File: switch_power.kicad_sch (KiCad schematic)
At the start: 31 parts, among them U1 LAN96455F-I/8MW

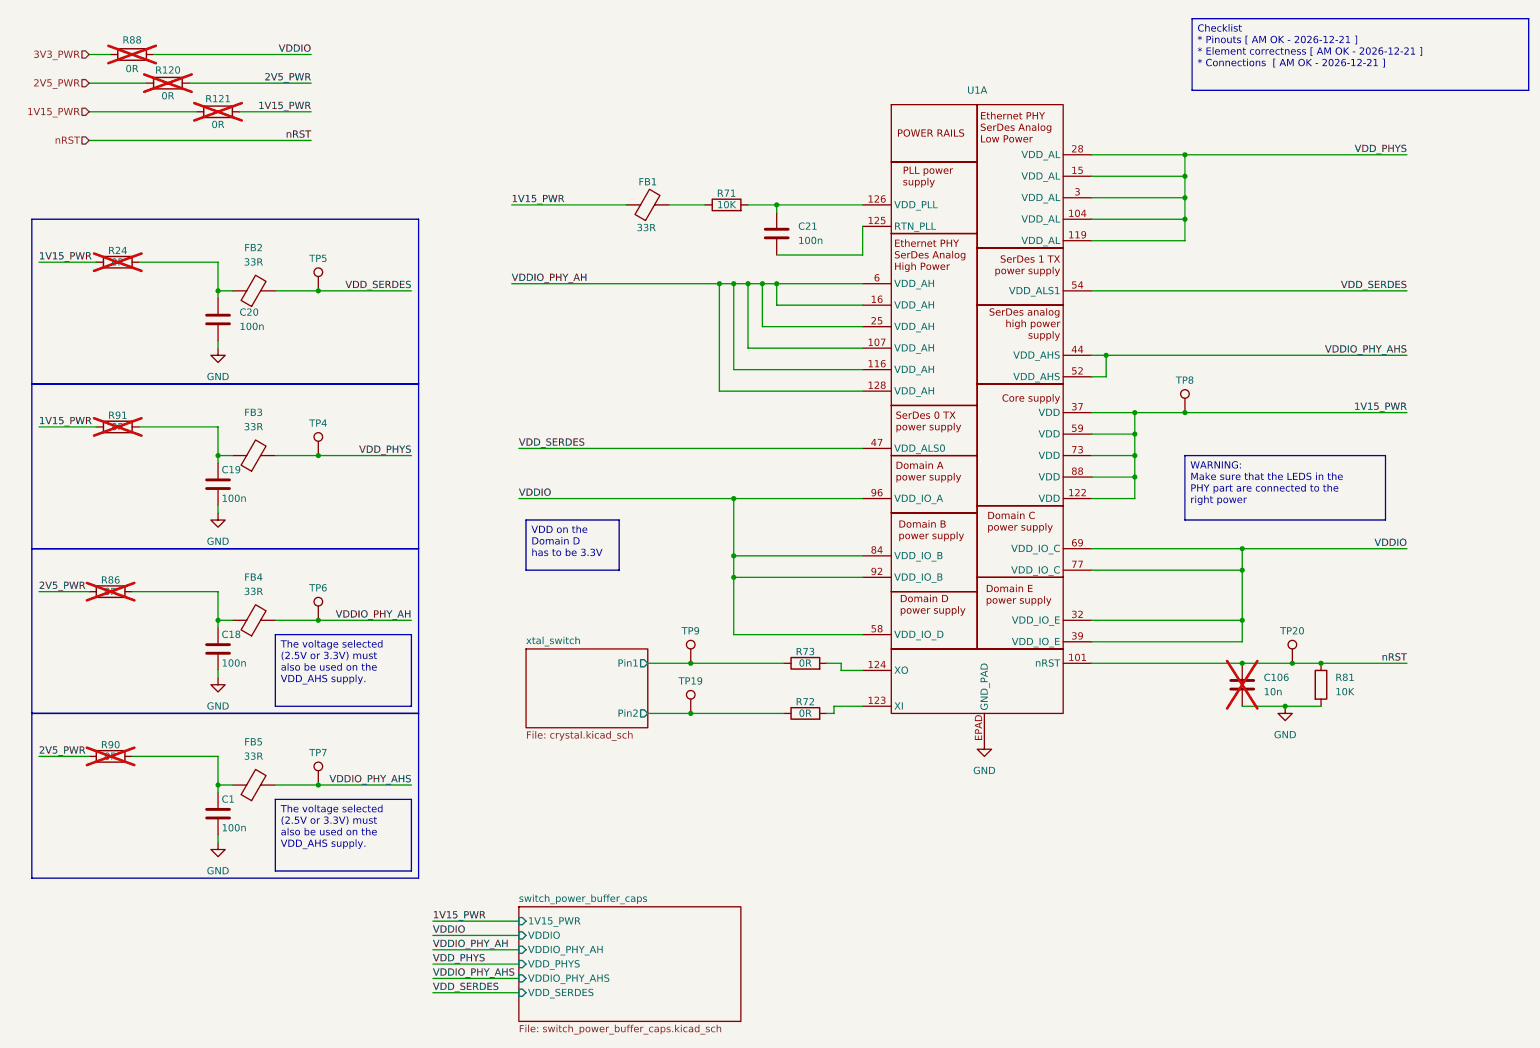
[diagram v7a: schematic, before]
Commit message: updates symbols and fixes ERC errors. Refs: #9
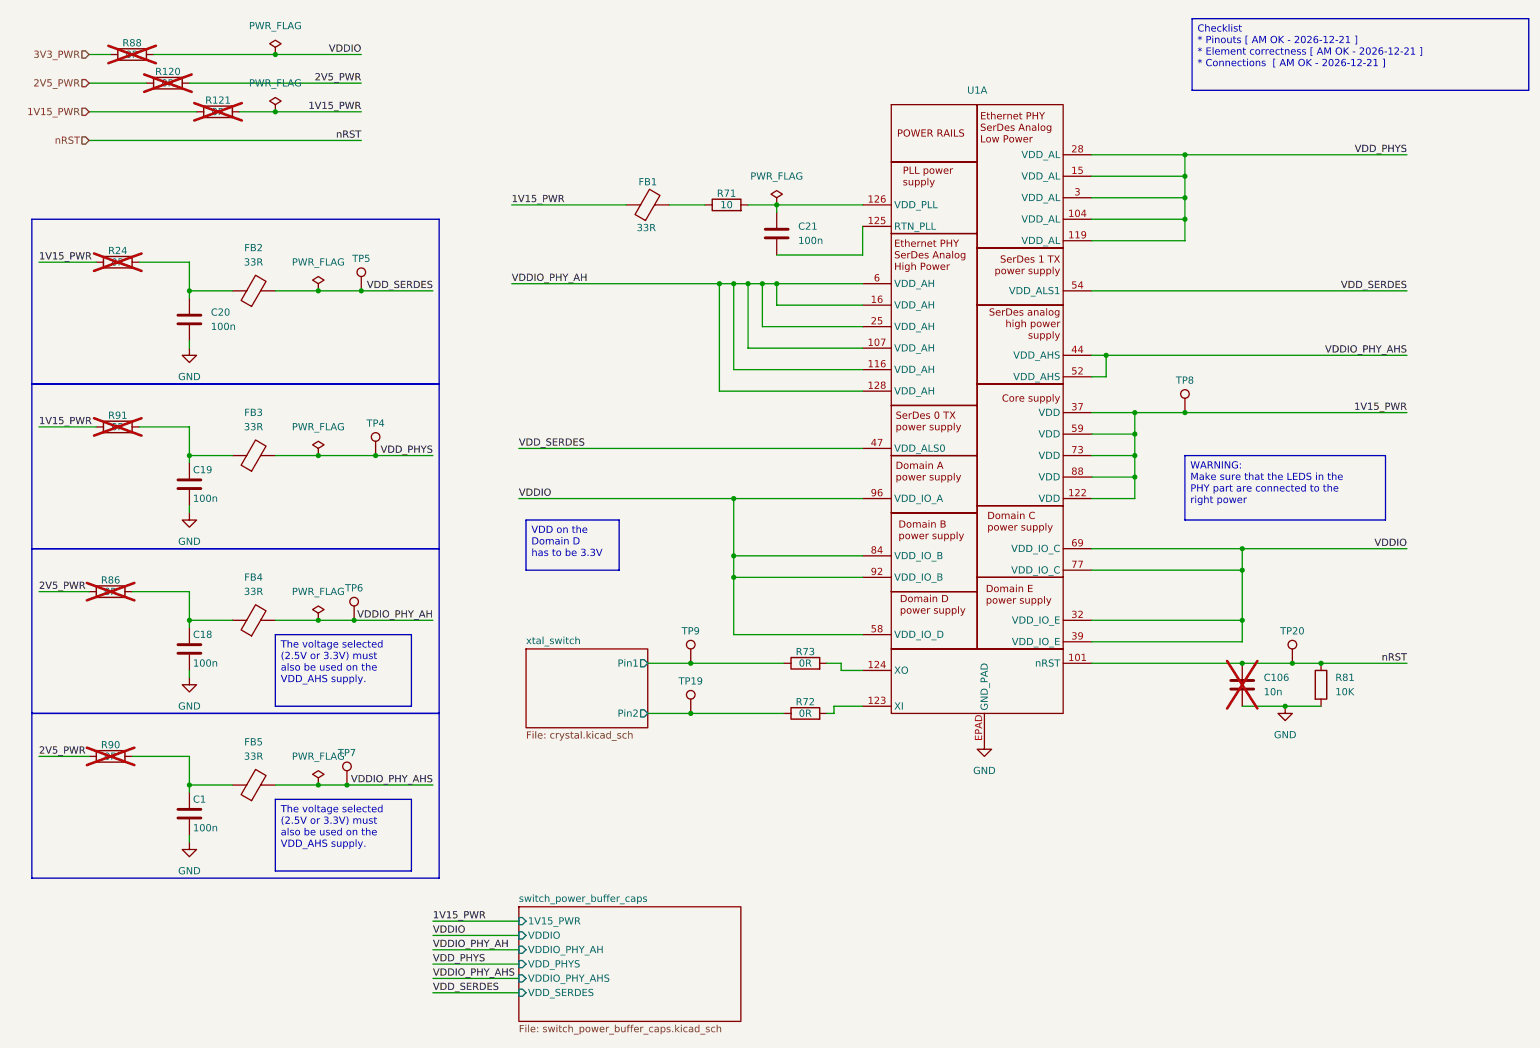
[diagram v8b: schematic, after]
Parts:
- R71: value 10K -> 10
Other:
- moved on the sheet: C1, C18, C19, C20, TP4, TP5, TP6, TP7
